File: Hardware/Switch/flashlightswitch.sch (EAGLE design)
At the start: 10 parts

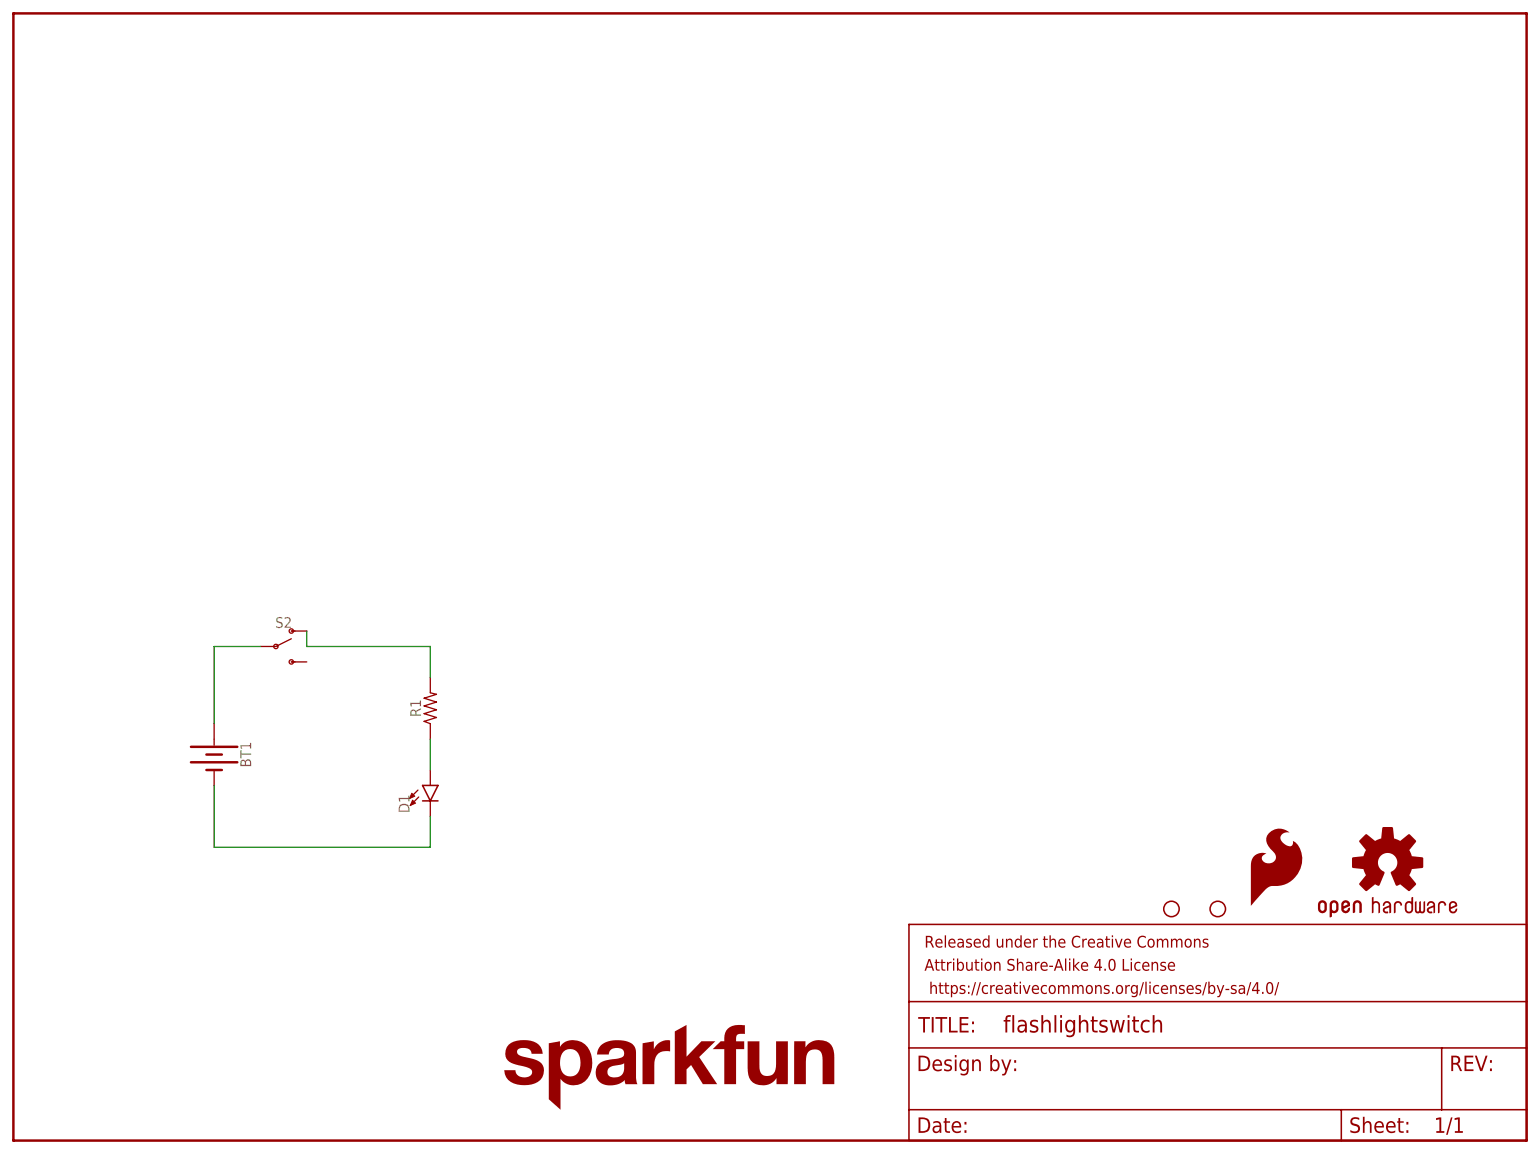
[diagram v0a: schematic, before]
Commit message: Updated before Proto Review
Made some tweaks to polish up the design a bit before the design review.
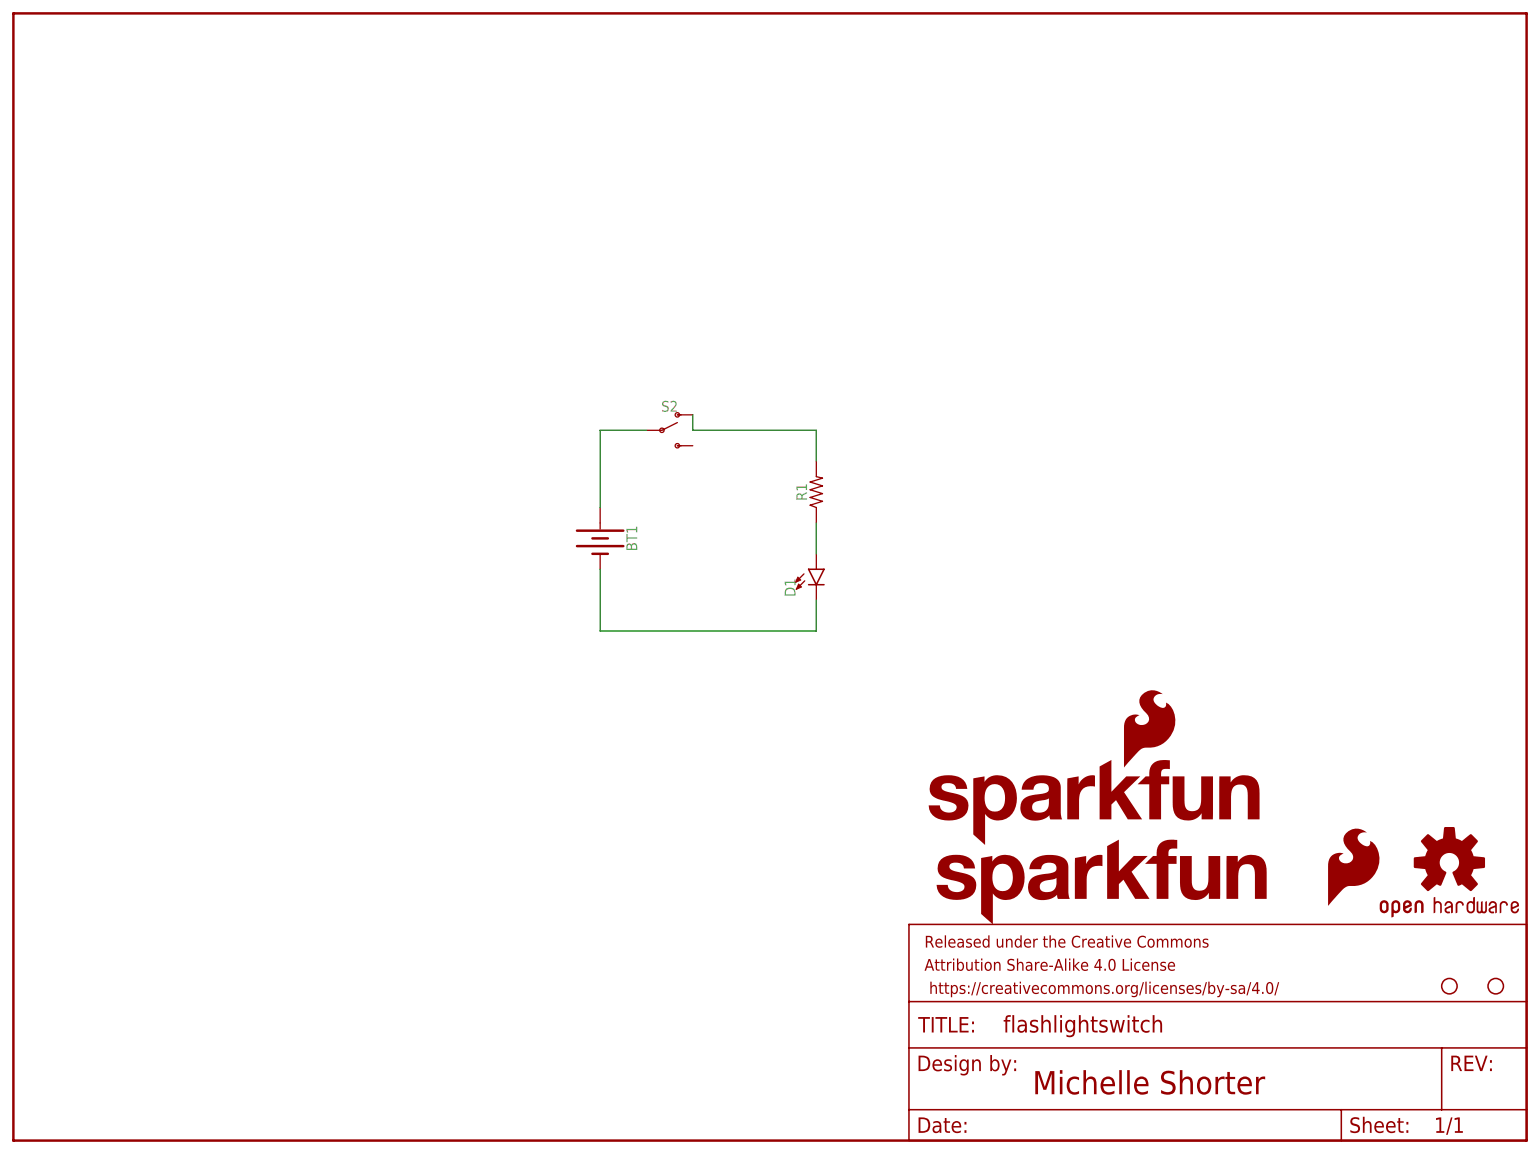
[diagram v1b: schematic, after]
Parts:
- added LOGO3: SFE_LOGO_NAME_FLAME.2_INCH, SparkFun-Aesthetics:SFE_LOGO_NAME_FLAME.2_INCH
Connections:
- net N$1 renamed BATT
- net N$4 renamed GND
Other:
- note added: "Michelle Shorter"
- moved on the sheet: BT1, D1, R1, S2
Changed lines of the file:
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@@
 <part name="S2" library="SparkFun-Switches" deviceset="SWITCH-SPDT" device="-PTH-11.6X4.0MM-KIT"/>
 <part name="LOGO4" library="SparkFun-Aesthetics" deviceset="SFE_LOGO_NAME" device=".1_INCH"/>
+<part name="LOGO3" library="SparkFun-Aesthetics" deviceset="SFE_LOGO_NAME_FLAME" device=".2_INCH"/>
 </parts>
 <sheets>
 <sheet>
 <plain>
+<text x="167.64" y="7.62" size="3.81" layer="94">Michelle Shorter</text>
 </plain>
 <instances>
-<instance part="BT1" gate="G$1" x="33.02" y="63.5" rot="R270"/>
+<instance part="BT1" gate="G$1" x="96.52" y="99.06" rot="R270"/>
 <instance part="FRAME1" gate="G$1" x="0" y="0"/>
 <instance part="FRAME1" gate="V" x="147.32" y="0"/>
-<instance part="LOGO1" gate="G$1" x="226.06" y="45.72"/>
-<instance part="D1" gate="G$1" x="68.58" y="58.42"/>
-<instance part="R1" gate="G$1" x="68.58" y="71.12" rot="R90"/>
-<instance part="LOGO2" gate="G$1" x="203.2" y="38.1"/>
-<instance part="H1" gate="G$1" x="198.12" y="38.1"/>
-<instance part="H2" gate="G$1" x="190.5" y="38.1"/>
-<instance part="S2" gate="1" x="43.18" y="81.28"/>
-<instance part="LOGO4" gate="G$1" x="78.74" y="5.08"/>
+<instance part="LOGO1" gate="G$1" x="236.22" y="45.72"/>
+<instance part="D1" gate="G$1" x="132.08" y="93.98"/>
+<instance part="R1" gate="G$1" x="132.08" y="106.68" rot="R90"/>
+<instance part="LOGO2" gate="G$1" x="215.9" y="38.1"/>
+<instance part="H1" gate="G$1" x="236.22" y="25.4"/>
+<instance part="H2" gate="G$1" x="243.84" y="25.4"/>
+<instance part="S2" gate="1" x="106.68" y="116.84"/>
+<instance part="LOGO4" gate="G$1" x="149.86" y="35.56"/>
+<instance part="LOGO3" gate="G$1" x="149.86" y="48.26"/>
 </instances>
 <busses>
 </busses>
 <nets>
-<net name="N$1" class="0">
+<net name="BATT" class="0">
 <segment>
-<wire x1="33.02" y1="81.28" x2="40.64" y2="81.28" width="0.1524" layer="91"/>
+<wire x1="96.52" y1="116.84" x2="104.14" y2="116.84" width="0.1524" layer="91"/>
 <pinref part="BT1" gate="G$1" pin="+"/>
-<wire x1="33.02" y1="81.28" x2="33.02" y2="68.58" width="0.1524" layer="91"/>
+<wire x1="96.52" y1="116.84" x2="96.52" y2="104.14" width="0.1524" layer="91"/>
 <pinref part="S2" gate="1" pin="P"/>
 </segment>
@@
 <net name="N$2" class="0">
 <segment>
-<wire x1="48.26" y1="81.28" x2="68.58" y2="81.28" width="0.1524" layer="91"/>
+<wire x1="111.76" y1="116.84" x2="132.08" y2="116.84" width="0.1524" layer="91"/>
 <pinref part="R1" gate="G$1" pin="2"/>
-<wire x1="68.58" y1="81.28" x2="68.58" y2="76.2" width="0.1524" layer="91"/>
+<wire x1="132.08" y1="116.84" x2="132.08" y2="111.76" width="0.1524" layer="91"/>
 <pinref part="S2" gate="1" pin="O"/>
-<wire x1="48.26" y1="83.82" x2="48.26" y2="81.28" width="0.1524" layer="91"/>
+<wire x1="111.76" y1="119.38" x2="111.76" y2="116.84" width="0.1524" layer="91"/>
 </segment>
 </net>
@@
 <pinref part="R1" gate="G$1" pin="1"/>
 <pinref part="D1" gate="G$1" pin="A"/>
-<wire x1="68.58" y1="66.04" x2="68.58" y2="60.96" width="0.1524" layer="91"/>
+<wire x1="132.08" y1="101.6" x2="132.08" y2="96.52" width="0.1524" layer="91"/>
 </segment>
 </net>
-<net name="N$4" class="0">
+<net name="GND" class="0">
 <segment>
 <pinref part="D1" gate="G$1" pin="C"/>
-<wire x1="68.58" y1="53.34" x2="68.58" y2="48.26" width="0.1524" layer="91"/>
-<wire x1="68.58" y1="48.26" x2="33.02" y2="48.26" width="0.1524" layer="91"/>
+<wire x1="132.08" y1="88.9" x2="132.08" y2="83.82" width="0.1524" layer="91"/>
+<wire x1="132.08" y1="83.82" x2="96.52" y2="83.82" width="0.1524" layer="91"/>
 <pinref part="BT1" gate="G$1" pin="-"/>
-<wire x1="33.02" y1="58.42" x2="33.02" y2="48.26" width="0.1524" layer="91"/>
+<wire x1="96.52" y1="93.98" x2="96.52" y2="83.82" width="0.1524" layer="91"/>
 </segment>
 </net>
